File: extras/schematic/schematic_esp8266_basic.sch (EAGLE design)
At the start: 19 parts, among them U1 SI4735-D60-GU, U2 ESP8266

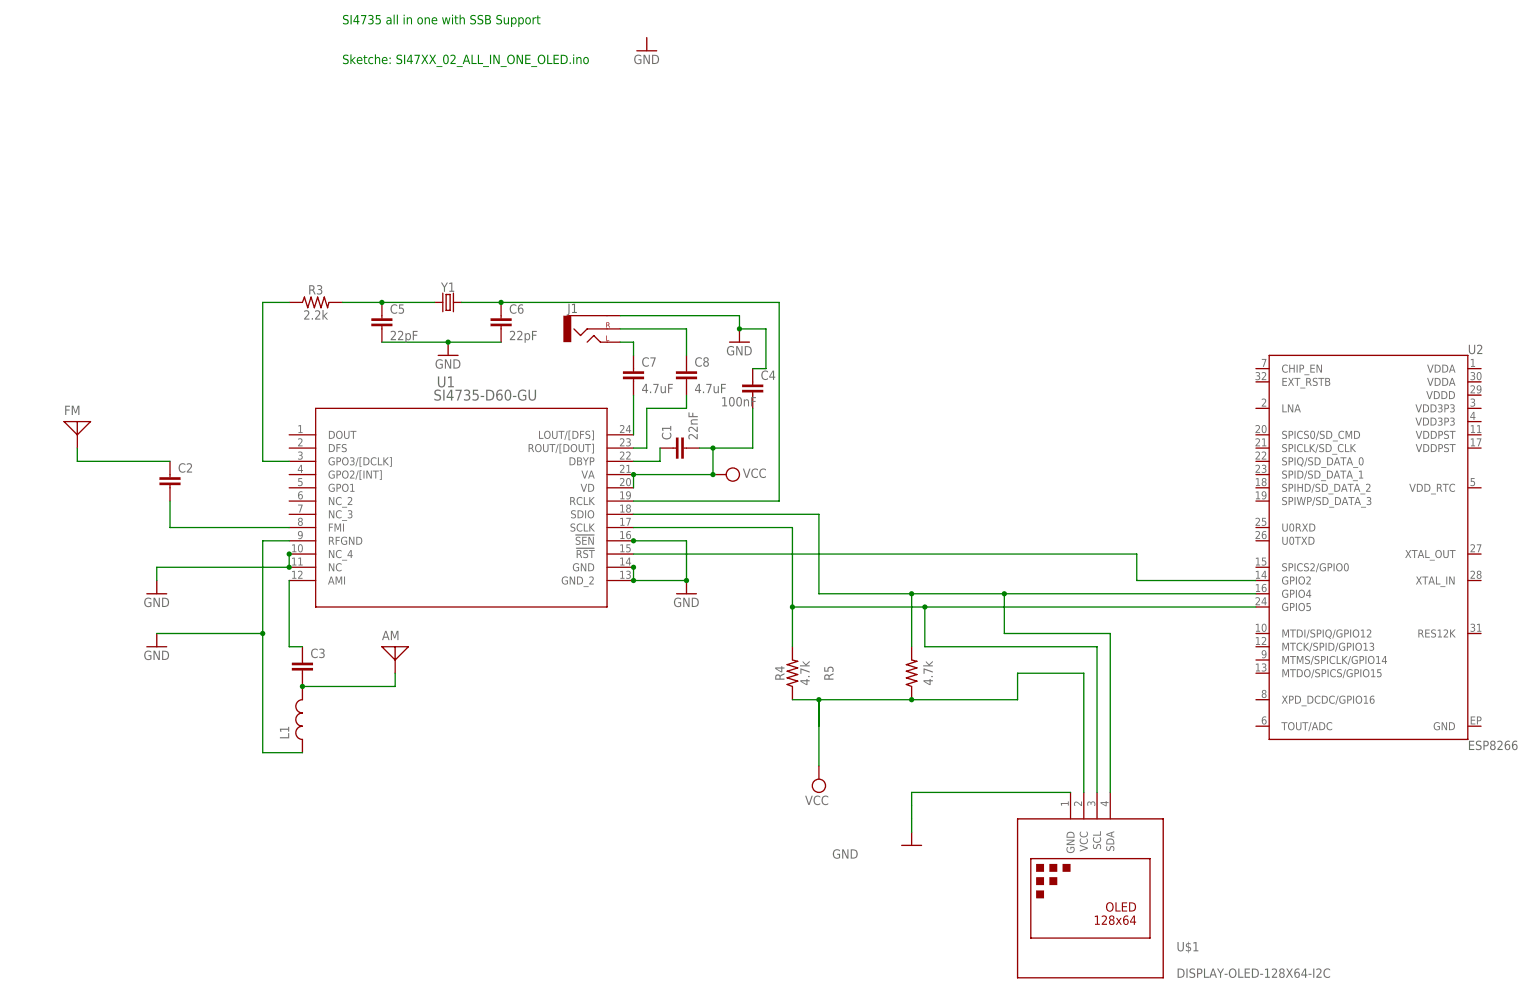
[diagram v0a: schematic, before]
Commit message: SI473X Arduino Library
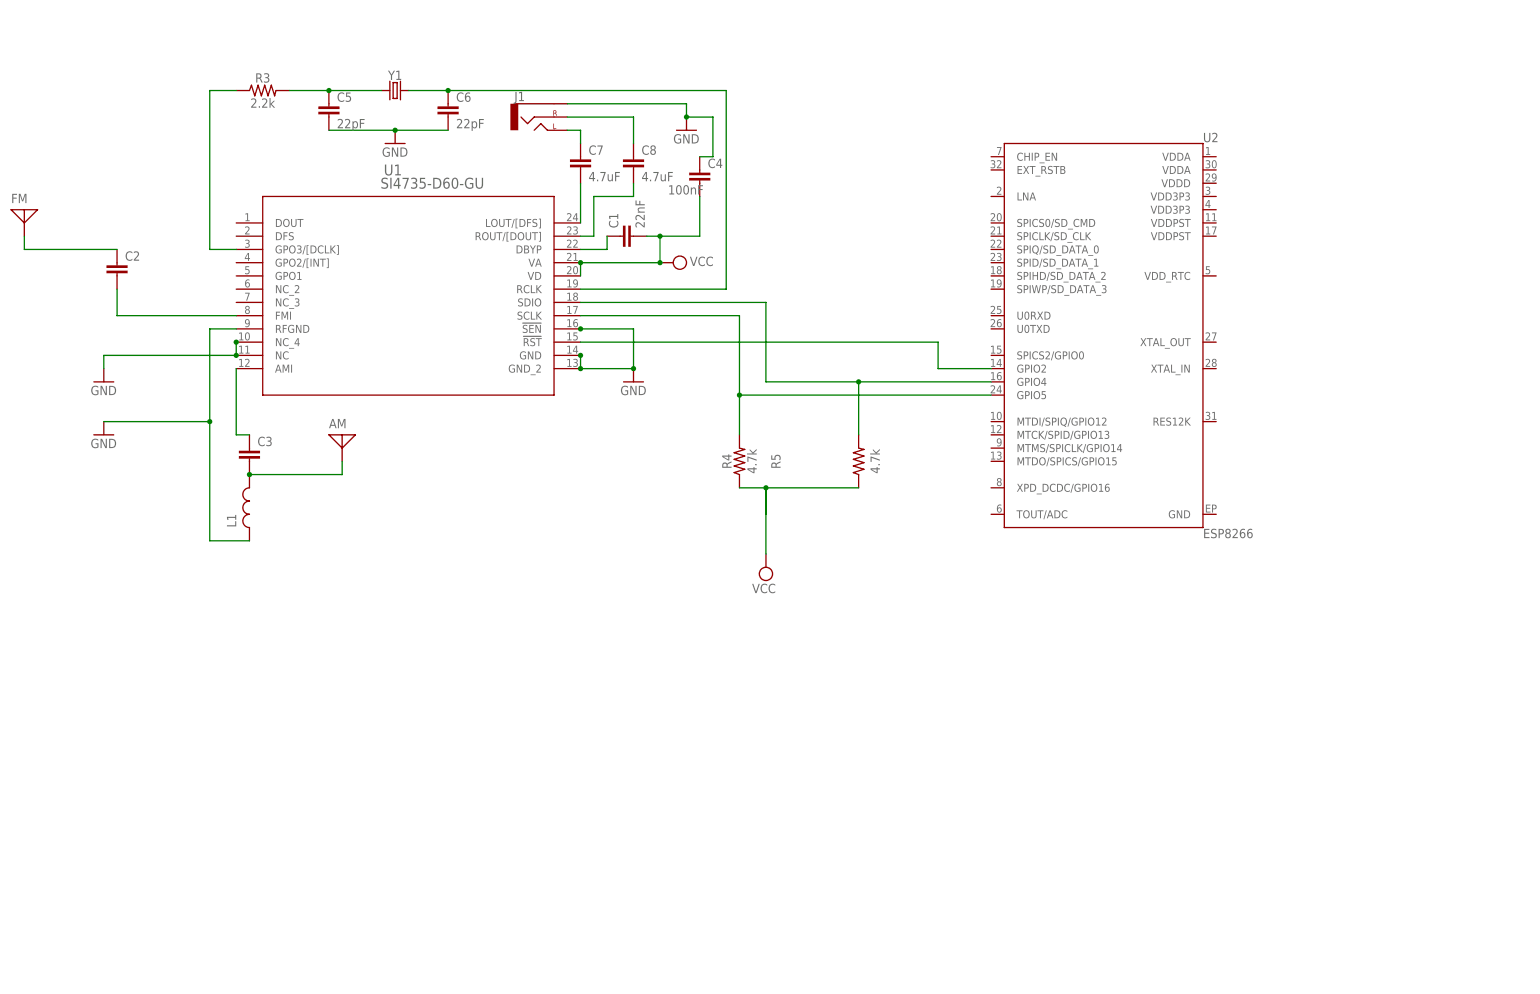
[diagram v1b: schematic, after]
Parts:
- removed U$1: DISPLAY-OLED-128X64-I2C, diy-modules:DISPLAY-OLED-128X64-I2C
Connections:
- net GND: no longer U$1.GND
- net N$2: no longer U$1.SDA
- net SDA: no longer U$1.SCL
- net VCC: no longer U$1.VCC
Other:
- note removed: "SI4735 all in one with SSB Support"
- note removed: "Sketche: SI47XX_02_ALL_IN_ONE_OLED.ino"
- moved on the sheet: AM, C1, C2, C3, C4, C5, C6, C7, C8, FM, J1, L1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
